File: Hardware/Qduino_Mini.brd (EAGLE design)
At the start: 38.1 x 25.4 mm, 45 parts, among them Q1 PFET, U1 ATMEGA32U41:1-LESS_PASTE, U2 MCP73831, U3 MAX17048, U4 TPS78233, U5 MIGHTYQ-L-SILK, U6 MIGHTYQ-S-SILK, U7 DNP, Y1 8MHZ

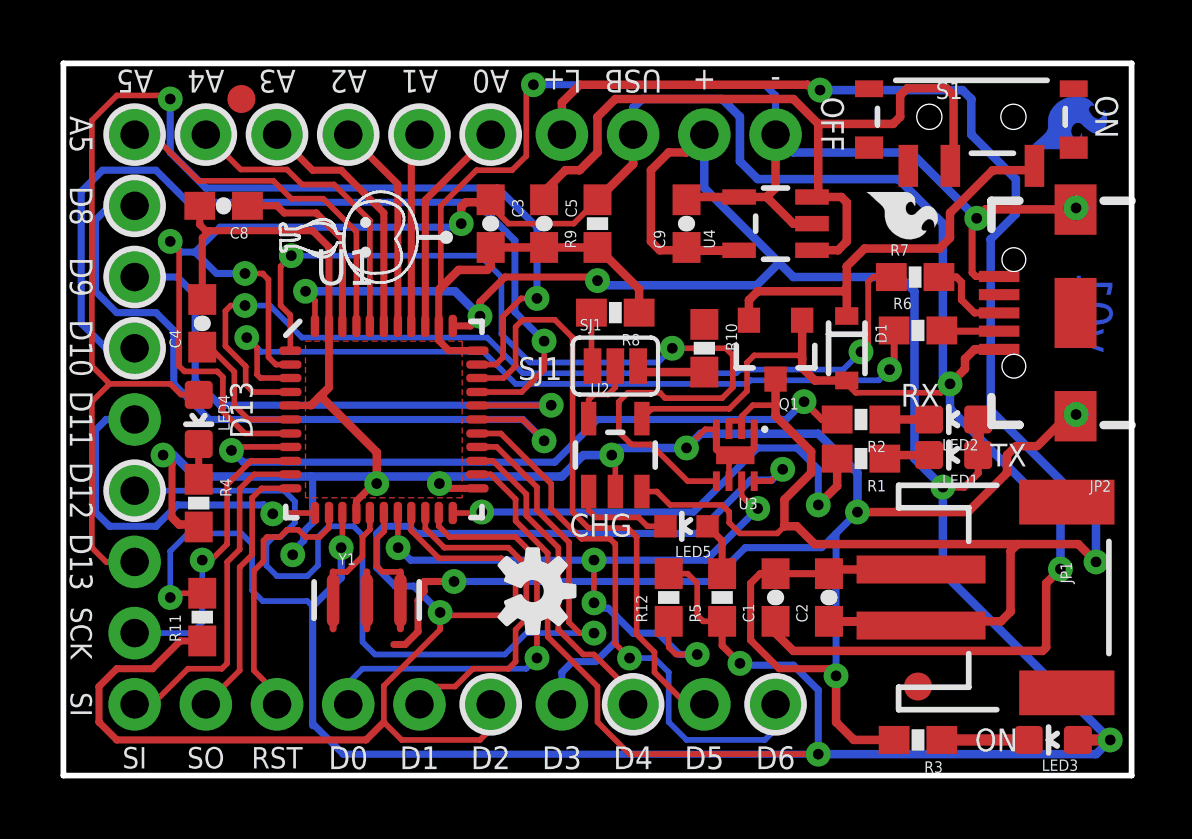
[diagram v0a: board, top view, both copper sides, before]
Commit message: Moved battery over to make rework easier.  In the process moved the power LED to the middle.  Also fixed RX/TX lines(D0/D1)
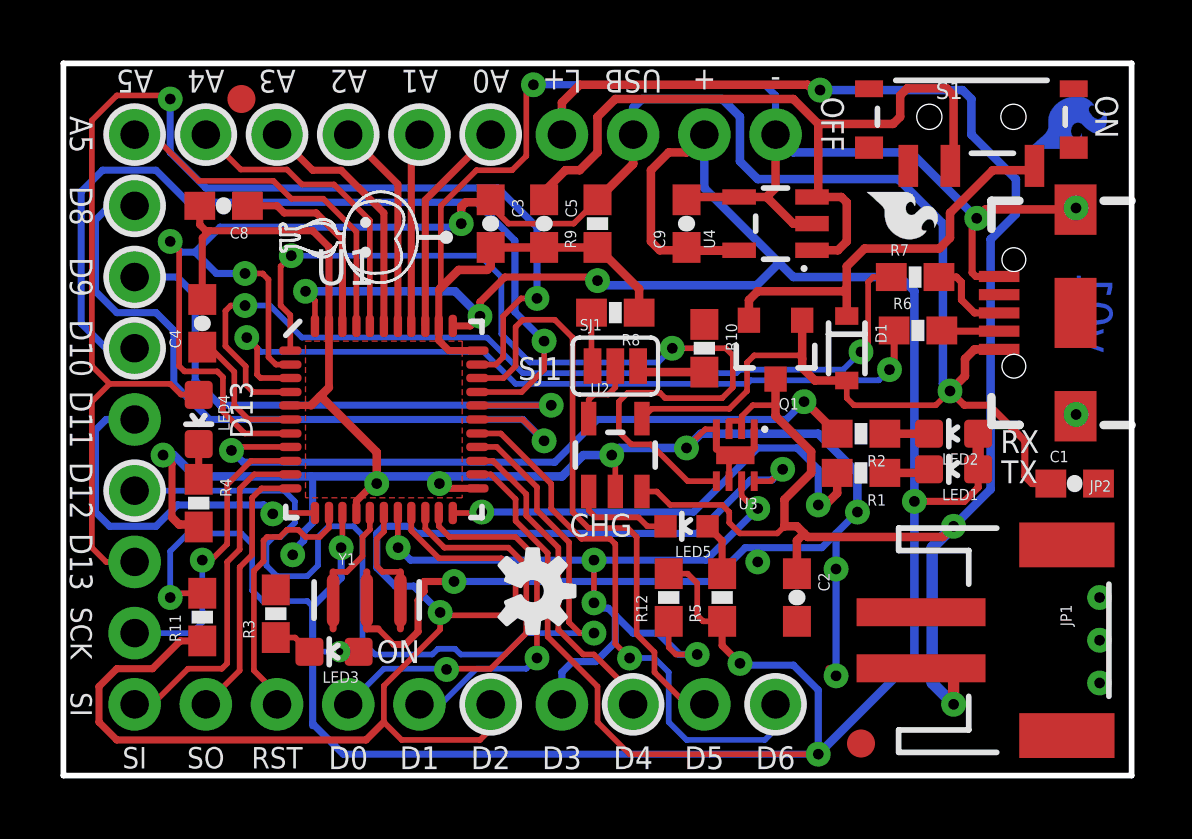
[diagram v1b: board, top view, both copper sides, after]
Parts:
- D1: value BAS16JTR -> 250mA/100V
- JP2: value USB_MICROB_PLUGCONN-11752 -> (none)
- LED1: value TX / YLW -> Yellow
- LED2: value RX / GRN -> GREEN
- LED3: value PWR / GRN -> GREEN
- LED4: value L / YLW -> Yellow
- moved LED3 25.8 mm to (9.65, 4.41)
- moved R3 23.3 mm to (7.58, 5.77), turned to 90 degrees
- moved C1 11.4 mm to (36.1, 10.4), turned to 0 degrees
- moved FID5 2.87 mm to (28.4, 1.14)
- moved JP1 1.52 mm to (34.3, 4.83)
- moved C2 1.14 mm to (26.2, 6.35), turned to 270 degrees
- moved R1 0.51 mm to (28.4, 10.8)
- moved LED1 0.51 mm to (31.8, 10.9)
- moved LED2 0.51 mm to (31.8, 12.2)
- moved R2 0.51 mm to (28.4, 12.2)
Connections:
- removed net RX: U1.20, U7.TX
- removed net TX: U1.21, U7.RX
- new net D0: U1.20, U7.D0
- new net D1: U1.21, U7.D1
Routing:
- net GND: track 168.4 -> 144.3 mm, vias 13 -> 18
- net TX: track 15.9 -> 0.00 mm, vias 1 -> 0
- net VBUS: track 98.6 -> 83.8 mm, vias 5 -> 4
- net D0: track 0.00 -> 14.5 mm, vias 0 -> 1
- net D1: track 0.00 -> 12.9 mm, vias 0 -> 1
- net RX: track 12.3 -> 0.00 mm
- net VCC: track 142.9 -> 132.8 mm
- net LIPO: track 74.6 -> 69.5 mm, vias 2 -> 3
- net N$12: track 3.10 -> 1.41 mm
